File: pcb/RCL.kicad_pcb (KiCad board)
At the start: 2 copper layers, 52 x 52 mm, 86 parts, among them J1 USB_C_Receptacle, J2 Conn_01x02_Pin, J3 Conn_01x05_Pin, Q1 BSP613, Q2 AO3416A, Q3 AO3416A, Q4 AO3416A, SW1 SW_SPDT, SW2 SW_DIP_x02, SW3 SW_Push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

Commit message: Add missing vendor(id)
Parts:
- R21, R24: value 27 -> 0
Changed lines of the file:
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@@
     (property "Sheetfile" "RCL.kicad_sch")
     (property "Sheetname" "")
+    (property "Vendor" "HTL")
+    (property "VendorId" "103607")
     (property "ki_description" "RGB LED with integrated controller")
     (property "ki_keywords" "RGB LED addressable 8bit pwm 5bit greyscale")
@@
     (property "Sheetfile" "RCL.kicad_sch")
     (property "Sheetname" "")
+    (property "Vendor" "HTL")
+    (property "VendorId" "101546")
     (property "ki_description" "Generic connector, single row, 01x05, script generated")
     (property "ki_keywords" "connector")
@@
     (property "Sheetfile" "RCL.kicad_sch")
     (property "Sheetname" "")
+    (property "Vendor" "HTL")
+    (property "VendorId" "103607")
     (property "ki_description" "RGB LED with integrated controller")
     (property "ki_keywords" "RGB LED addressable 8bit pwm 5bit greyscale")
@@
     (property "Sheetfile" "RCL.kicad_sch")
     (property "Sheetname" "")
+    (property "Vendor" "HTL")
+    (property "VendorId" "103607")
     (property "ki_description" "RGB LED with integrated controller")
     (property "ki_keywords" "RGB LED addressable 8bit pwm 5bit greyscale")
@@
     (property "Sheetfile" "RCL.kicad_sch")
     (property "Sheetname" "")
+    (property "Vendor" "HTL")
+    (property "VendorId" "103607")
     (property "ki_description" "RGB LED with integrated controller")
     (property "ki_keywords" "RGB LED addressable 8bit pwm 5bit greyscale")
@@
     (property "Sheetfile" "RCL.kicad_sch")
     (property "Sheetname" "")
+    (property "Vendor" "HTL")
+    (property "VendorId" "103607")
     (property "ki_description" "RGB LED with integrated controller")
     (property "ki_keywords" "RGB LED addressable 8bit pwm 5bit greyscale")
@@
     (property "Sheetfile" "RCL.kicad_sch")
     (property "Sheetname" "")
+    (property "Vendor" "HTL")
+    (property "VendorId" "103607")
     (property "ki_description" "RGB LED with integrated controller")
     (property "ki_keywords" "RGB LED addressable 8bit pwm 5bit greyscale")
@@
     (property "Sheetfile" "RCL.kicad_sch")
     (property "Sheetname" "")
+    (property "Vendor" "HTL")
+    (property "VendorId" "103607")
     (property "ki_description" "RGB LED with integrated controller")
     (property "ki_keywords" "RGB LED addressable 8bit pwm 5bit greyscale")
@@
     (property "Sheetfile" "RCL.kicad_sch")
     (property "Sheetname" "")
+    (property "Vendor" "HTL")
+    (property "VendorId" "103607")
     (property "ki_description" "RGB LED with integrated controller")
     (property "ki_keywords" "RGB LED addressable 8bit pwm 5bit greyscale")
@@
     (property "Sheetfile" "RCL.kicad_sch")
     (property "Sheetname" "")
-    (property "Vendor" "HTL")
-    (property "VendorId" "102920")
+    (property "Vendor" "DigiKey")
+    (property "VendorId" "RMCF0603ZT0R00CT-ND")
     (property "ki_description" "Resistor")
     (property "ki_keywords" "R res resistor")
@@
         (effects (font (size 0.6 0.6) (thickness 0.12)) (justify mirror))
     )
-    (fp_text value "27" (at 0 1.27 90) (layer "B.Fab")
+    (fp_text value "0" (at 0 1.27 90) (layer "B.Fab")
         (effects (font (size 1 1) (thickness 0.15)) (justify mirror))
     )
@@
     (property "Sheetfile" "RCL.kicad_sch")
     (property "Sheetname" "")
-    (property "Vendor" "HTL")
-    (property "VendorId" "102920")
+    (property "Vendor" "DigiKey")
+    (property "VendorId" "RMCF0603ZT0R00CT-ND")
     (property "ki_description" "Resistor")
     (property "ki_keywords" "R res resistor")
@@
         (effects (font (size 0.6 0.6) (thickness 0.12)) (justify mirror))
     )
-    (fp_text value "27" (at 0 -1.43 90) (layer "B.Fab")
+    (fp_text value "0" (at 0 -1.43 90) (layer "B.Fab")
         (effects (font (size 1 1) (thickness 0.15)) (justify mirror))
     )
@@
     (property "Sheetfile" "RCL.kicad_sch")
     (property "Sheetname" "")
+    (property "Vendor" "DigiKey")
+    (property "VendorId" "150-MCP2221AT-I/SLCT-ND")
     (property "ki_description" "USB to I2C/UART Protocol Converter with GPIO, SOIC-14")
     (property "ki_keywords" "USB I2C UART Converter Bridge")

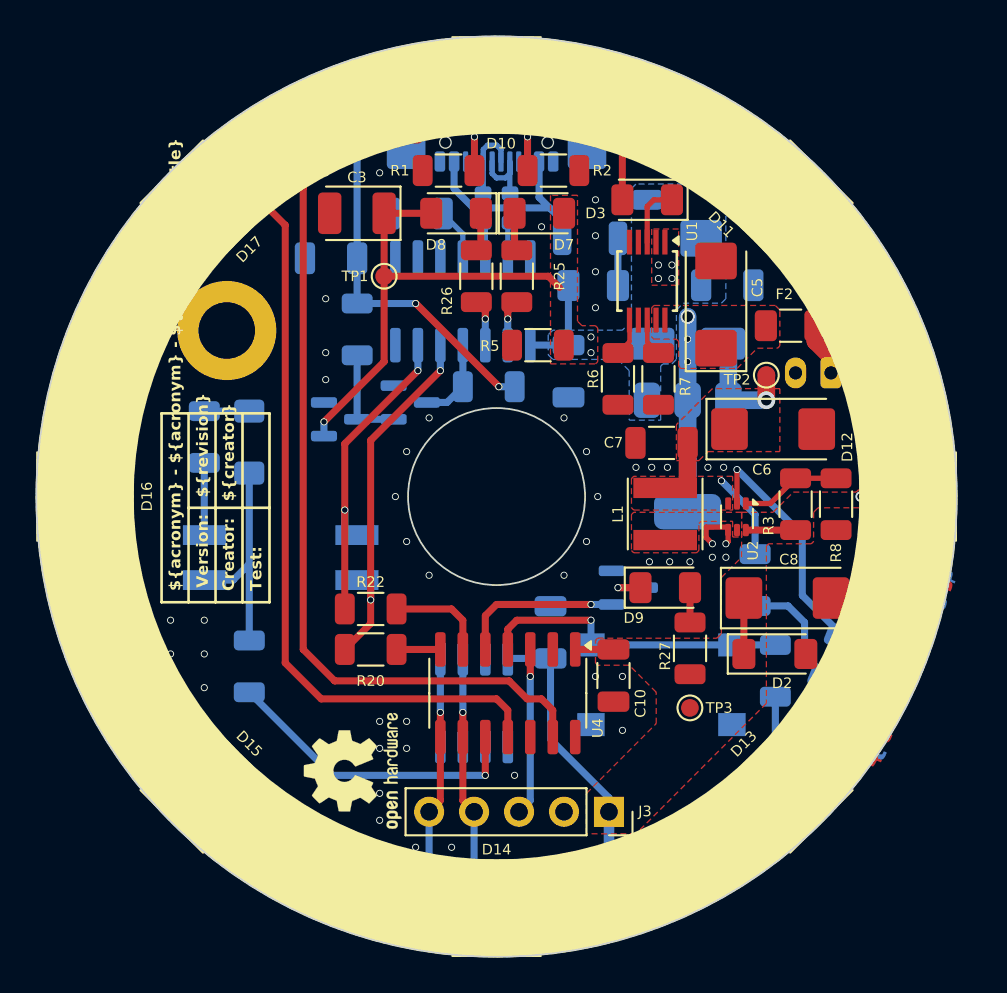
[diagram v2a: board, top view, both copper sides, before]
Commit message: Increase KiCAD version
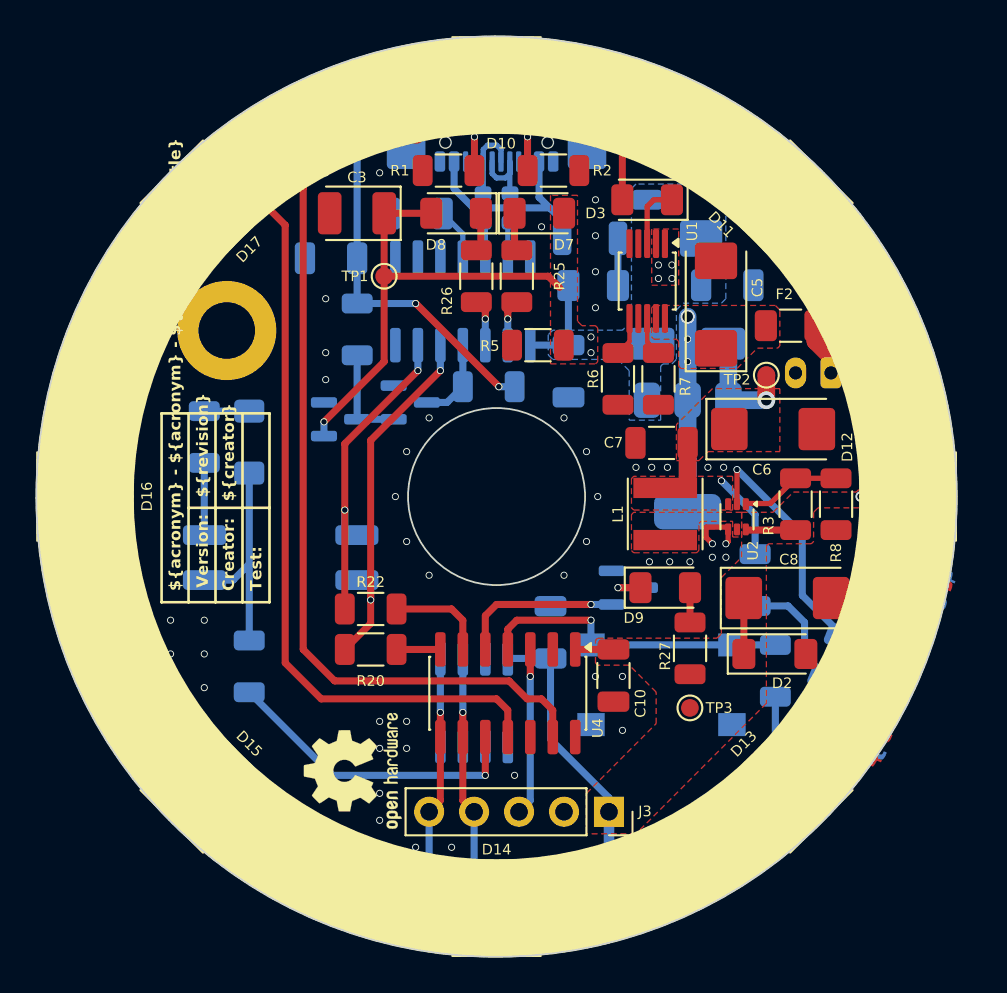
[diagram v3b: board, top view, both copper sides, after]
